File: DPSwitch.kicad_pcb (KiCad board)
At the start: 4 copper layers, 71 x 74.5 mm, 43 parts, among them J1 USB_OTG, J2 USB_OTG, J3 DP_47272, J4 DP_47272, J5 DP_47272, J6 USB_A, SW1 SEL_A, SW2 SEL_B, U1 HD3SS215, U2 74LVC2G00DC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

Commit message: Rev1 for manufacture
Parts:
- C16: footprint Capacitors_SMD:C_0603_HandSoldering -> Capacitors_SMD:C_0805_HandSoldering
- D1, D2: value D_Small -> BAT54GWJ; footprint Diodes_SMD:D_SC-80_HandSoldering -> Diodes_SMD:D_SOD-123
- D4: footprint LEDs:LED_0603_HandSoldering -> Visclib:wolfpaw-0.3-illuminated
- moved D5 64.7 mm to (87.4, 46.5), turned to 270 degrees
- moved SW2 63.2 mm to (80.3, 46.5), turned to 180 degrees
- moved D1 56.4 mm to (71.5, 98.9), turned to 90 degrees
- moved D2 50.3 mm to (71.5, 45.2), turned to 90 degrees
- moved R9 44.8 mm to (89.5, 46.5), turned to 90 degrees
- moved D4 33.5 mm to (81.8, 72.8), turned to 270 degrees
- moved J6 31.8 mm to (119.2, 86.5)
- moved C15 30.1 mm to (100.8, 81.8), turned to 180 degrees
- moved U3 29.6 mm to (100.8, 78.5), turned to 270 degrees
- moved C16 29.1 mm to (100.8, 75.2), turned to 180 degrees
- moved R10 24.1 mm to (89.8, 98.5), turned to 90 degrees
- moved R11 20.0 mm to (82.5, 78.0), turned to 180 degrees
- moved U2 11.2 mm to (108.2, 78.0)
- moved R8 10.1 mm to (105.2, 78.0), turned to 90 degrees
- moved SW1 9.92 mm to (80.4, 98.5)
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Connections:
- J1 pad 1: Net-(D2-Pad2) -> Net-(D1-Pad2)
- J2 pad 1: Net-(D1-Pad2) -> Net-(D2-Pad2)
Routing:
- net VDD: track 0.00 -> 113.8 mm
- net +3V3: track 97.8 -> 164.3 mm, vias 4 -> 9
- net /SW_B: track 0.00 -> 63.6 mm, vias 0 -> 2
- net /SW_A: track 0.00 -> 53.1 mm, vias 0 -> 2
- net /DX_SEL: track 17.3 -> 53.3 mm, vias 0 -> 3
- net /~Q: track 0.00 -> 34.3 mm, vias 0 -> 2
- net GND: track 60.3 -> 93.1 mm, vias 33 -> 48
- net /UC_P: track 44.5 -> 61.1 mm
- net /UC_N: track 44.5 -> 61.1 mm
- net Net-(D4-Pad1): track 0.00 -> 12.6 mm, vias 0 -> 1
- net /UB_N: track 65.0 -> 74.5 mm
- net /DA3_P: track 29.1 -> 38.3 mm
- net /DA3_N: track 29.1 -> 38.4 mm
- net /DA1_N: track 29.3 -> 38.5 mm
- net /DA1_P: track 29.2 -> 38.4 mm
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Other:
- board size 71 x 74.5 mm -> 71 x 64 mm
- board text added: "OwO What's That?"
- board text added: "OwO What's This?"

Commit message: Added moth
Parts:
- added LOGO1: Moth, Project:moth, B.Cu at (100.0, 72.0)
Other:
- board text added: "DisplayPort Switch"
- board text added: "Jared Sanson | jared.geek.nz"
- board text added: "Puriri"
- board text removed: "OwO What's That?"
- board text removed: "OwO What's This?"

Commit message: Final gerbers rev1.2
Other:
- rule solder_mask_min_width: 0.25 -> 0.05
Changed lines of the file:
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@@
     (pad_drill 0.762)
     (pad_to_mask_clearance 0.051)
-    (solder_mask_min_width 0.25)
+    (solder_mask_min_width 0.05)
     (aux_axis_origin 0 0)
     (visible_elements 7FFFFFFF)
     (pcbplotparams
-      (layerselection 0x010fc_ffffffff)
+      (layerselection 0x010f0_ffffffff)
       (usegerberextensions false)
       (usegerberattributes false)
@@
       (plotinvisibletext false)
       (padsonsilk false)
-      (subtractmaskfromsilk false)
+      (subtractmaskfromsilk true)
       (outputformat 1)
       (mirror false)
-      (drillshape 1)
+      (drillshape 0)
       (scaleselection 1)
-      (outputdirectory ""))
+      (outputdirectory "gerbers"))
   )
   (net 0 "")

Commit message: Tidy up fabrication layer
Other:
- board text added: "100n x8"

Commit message: r2 - Swap USB A/B inputs, fix inverted flip-flop logic
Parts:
- moved D1 53.7 mm to (71.5, 45.2)
- moved D2 53.5 mm to (71.5, 98.8)
- moved J1 52.0 mm to (63.5, 46.5)
- moved J2 52.0 mm to (63.5, 98.5)
- moved R8 6.01 mm to (111.2, 77.8)
- moved R7 5.76 mm to (105.2, 77.8)
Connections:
- R7 pad 1: /SW_A -> +3V3
- R7 pad 2: GND -> /SW_B
- R8 pad 1: /SW_B -> +3V3
- R8 pad 2: GND -> /SW_A
- SW1 pad 1: +3V3 -> GND
- SW2 pad 1: +3V3 -> GND
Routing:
- net +3V3: track 164.3 -> 107.8 mm, vias 9 -> 7
- net /UA_N: track 34.3 -> 67.4 mm
- net /UA_P: track 34.3 -> 67.4 mm
- net /UB_N: track 74.5 -> 41.9 mm
- net /UB_P: track 74.5 -> 41.9 mm
- net GND: track 93.1 -> 105.9 mm, vias 48 -> 57
- net /UC_N: track 61.1 -> 58.3 mm
- net /UC_P: track 61.1 -> 58.3 mm
- net Net-(D1-Pad2): track 5.30 -> 5.94 mm
- net Net-(D2-Pad2): track 5.94 -> 5.32 mm
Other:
- board text added: "r2"

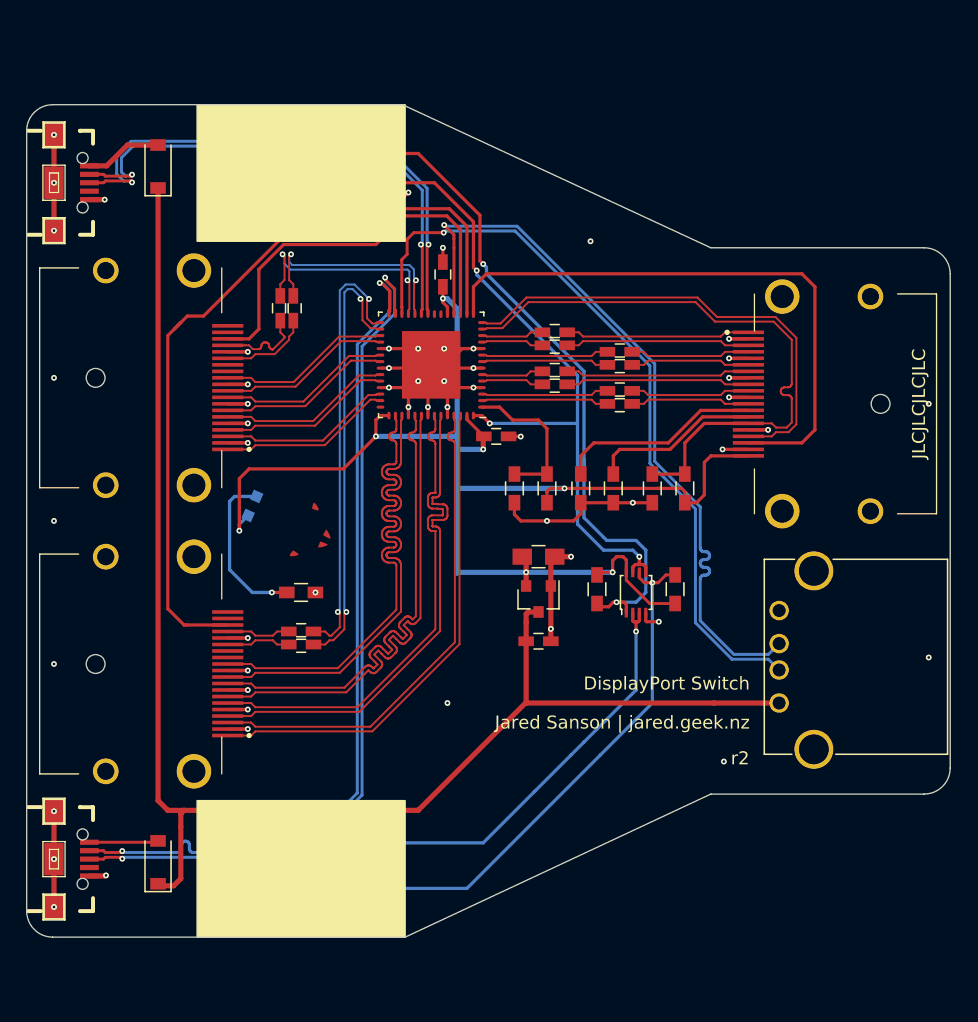
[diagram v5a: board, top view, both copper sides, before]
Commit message: Add testpads, 0R resistors to allow reconfiguration, and OSHW logo
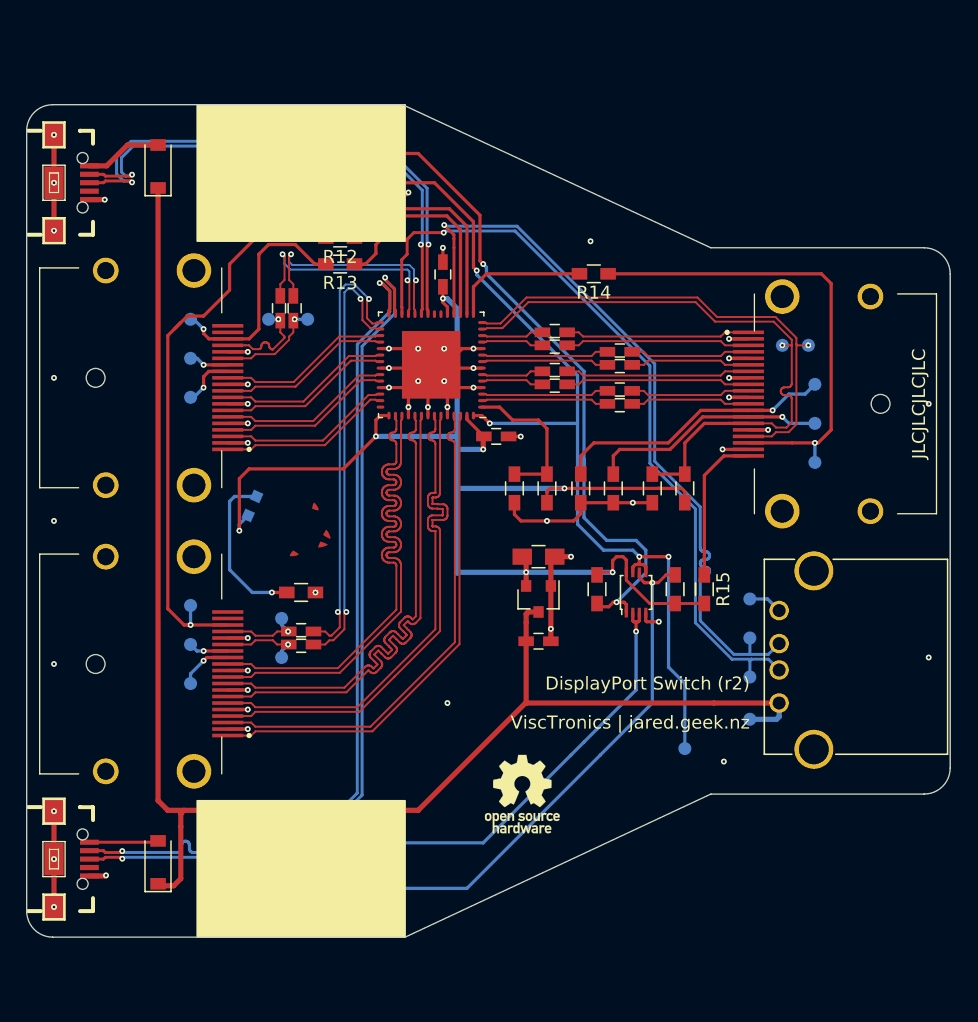
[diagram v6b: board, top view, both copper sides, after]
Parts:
- added LOGO2: OSHW, Symbols:OSHW-Logo_5.7x6mm_SilkScreen, F.Cu at (99.5, 93.5)
- added R12: 0R, Resistors_SMD:R_0603_HandSoldering, F.Cu at (85.5, 50.8)
- added R13: 0R, Resistors_SMD:R_0603_HandSoldering, F.Cu at (85.5, 52.8)
- added R14: 0R, Resistors_SMD:R_0603_HandSoldering, F.Cu at (105.0, 53.5)
- added R15: 0R, Resistors_SMD:R_0603_HandSoldering, F.Cu at (113.5, 77.8)
- added TP1: CFG1, Visclib:TP-1MM, B.Cu at (74.0, 85.0)
- added TP10: HPD, Visclib:TP-1MM, B.Cu at (74.0, 57.0)
- added TP11: VIN, Visclib:TP-1MM, B.Cu at (117.0, 87.8)
- added TP13: DX_SEL, Visclib:TP-1MM, B.Cu at (112.0, 90.0)
- added TP14: CFG1, Visclib:TP-1MM, B.Cu at (122.0, 62.0)
- added TP15: AUXP, Visclib:TP-1MM, B.Cu at (119.5, 59.0)
- added TP16: AUXN, Visclib:TP-1MM, B.Cu at (121.5, 59.0)
- added TP17: HPD, Visclib:TP-1MM, B.Cu at (122.0, 68.0)
- added TP18: CFG2, Visclib:TP-1MM, B.Cu at (122.0, 65.0)
- added TP19: USB_DP, Visclib:TP-1MM, B.Cu at (117.0, 81.5)
- added TP2: CFG2, Visclib:TP-1MM, B.Cu at (74.0, 82.0)
- added TP20: USB_DN, Visclib:TP-1MM, B.Cu at (117.0, 84.5)
- added TP21: GND, Visclib:TP-1MM, B.Cu at (117.0, 78.5)
- added TP3: CFG1, Visclib:TP-1MM, B.Cu at (74.0, 63.0)
- added TP4: CFG2, Visclib:TP-1MM, B.Cu at (74.0, 60.0)
- added TP5: AUXP, Visclib:TP-1MM, B.Cu at (81.0, 83.0)
- added TP6: AUXN, Visclib:TP-1MM, B.Cu at (81.0, 80.0)
- added TP7: HPD, Visclib:TP-1MM, B.Cu at (74.0, 79.0)
- added TP8: AUXP, Visclib:TP-1MM, B.Cu at (83.0, 57.0)
- added TP9: AUXN, Visclib:TP-1MM, B.Cu at (80.0, 57.0)
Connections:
- J3 pad 18: /HPDA -> Net-(J3-Pad18)
- J4 pad 18: /HPDB -> Net-(J4-Pad18)
- J5 pad 18: /HPDC -> Net-(J5-Pad18)
- J5 pad 20: +3V3 -> Net-(J5-Pad20)
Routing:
- net Net-(J3-Pad18): track 0.00 -> 44.8 mm, vias 0 -> 1
- net /HPDA: track 61.2 -> 16.9 mm
- net Net-(J5-Pad18): track 0.00 -> 37.0 mm, vias 0 -> 1
- net /HPDC: track 45.7 -> 10.7 mm
- net Net-(J4-Pad18): track 0.00 -> 18.2 mm, vias 0 -> 1
- net /DX_SEL: track 53.3 -> 70.9 mm, vias 3 -> 4
- net /HPDB: track 31.4 -> 17.0 mm
- net Net-(J5-Pad20): track 0.00 -> 11.7 mm
- net /CFG1: track 15.7 -> 21.7 mm, vias 0 -> 1
- net +3V3: track 107.8 -> 102.2 mm
- net /CFG2: track 13.0 -> 18.3 mm, vias 0 -> 1
- net Net-(J4-Pad13): track 0.00 -> 4.18 mm, vias 0 -> 1
- net Net-(J3-Pad13): track 0.00 -> 4.13 mm, vias 0 -> 1
- net VDD: track 113.8 -> 117.2 mm
- net GND: track 105.9 -> 109.2 mm
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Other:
- board text added: "DisplayPort Switch (r2)"
- board text added: "ViscTronics | jared.geek.nz"
- board text removed: "DisplayPort Switch"
- board text removed: "Jared Sanson | jared.geek.nz"
- board text removed: "r2"
